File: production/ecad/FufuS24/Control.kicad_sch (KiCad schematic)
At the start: 28 parts, among them IC1 NLVPCA9535EDTR2G, J2 Conn_01x02, U1 RP2040, U2 W25Q128JVS

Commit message: Made GPIO changes
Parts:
- removed R29: 4.7k, footprints:RESC2012X60N, symbol Device:R
- added R24: 4.7k, footprints:RESC2012X60N, symbol Device:R
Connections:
- net +3.3V: now also R24.1
- net Heat_PWM1: now also U1.31 (GPIO20); no longer IC1.18 (IO1_5)
- net SCL_EXT: now also R19.2
- net SDA_EXT: now also R24.2
- net Watersense1_Mode: now also IC1.10 (IO0_6); no longer U1.32 (GPIO21)
- net Watersense1_Read: now also IC1.11 (IO0_7); no longer U1.31 (GPIO20)
- net Watersense2_Mode: now also IC1.8 (IO0_4); no longer U1.35 (GPIO23)
- net Watersense2_Read: now also IC1.9 (IO0_5); no longer U1.34 (GPIO22)
- net I2C0_SCL: no longer names the net of IC1.19 (IO1_6)
- net I2C0_SDA: no longer names the net of IC1.20 (IO1_7)
- net I2C0_SDA: no longer R19.2
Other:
- moved on the sheet: IC1

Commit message: Big layout push
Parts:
- removed IC1: NLVPCA9535EDTR2G, footprints:SOP65P640X120-24N, symbol NLVPCA9535EDTR2G:NLVPCA9535EDTR2G
- removed R41, R42: 1.75k, footprints:RESC2012X60N, symbol Device:R
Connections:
- net AD0_EXT is gone; now on net Piezo_Enable: U1.4 (GPIO2)
- net AD2_EXT is gone; now on net Motor_BIN1: U1.6 (GPIO4)
- net I2C1_SCL_DVI is gone; now on net HOT_LED_NEG: U1.30 (GPIO19)
- net I2C1_SDA_DVI is gone; now on net HOT_LED_POS: U1.29 (GPIO18)
- net Pump_Enable: now also U1.32 (GPIO21)
- net Watersense1_Read: now also U1.35 (GPIO23)
- net Watersense2_Read: now also U1.34 (GPIO22)
- net AD1_EXT: no longer names the net of U1.5 (GPIO3)

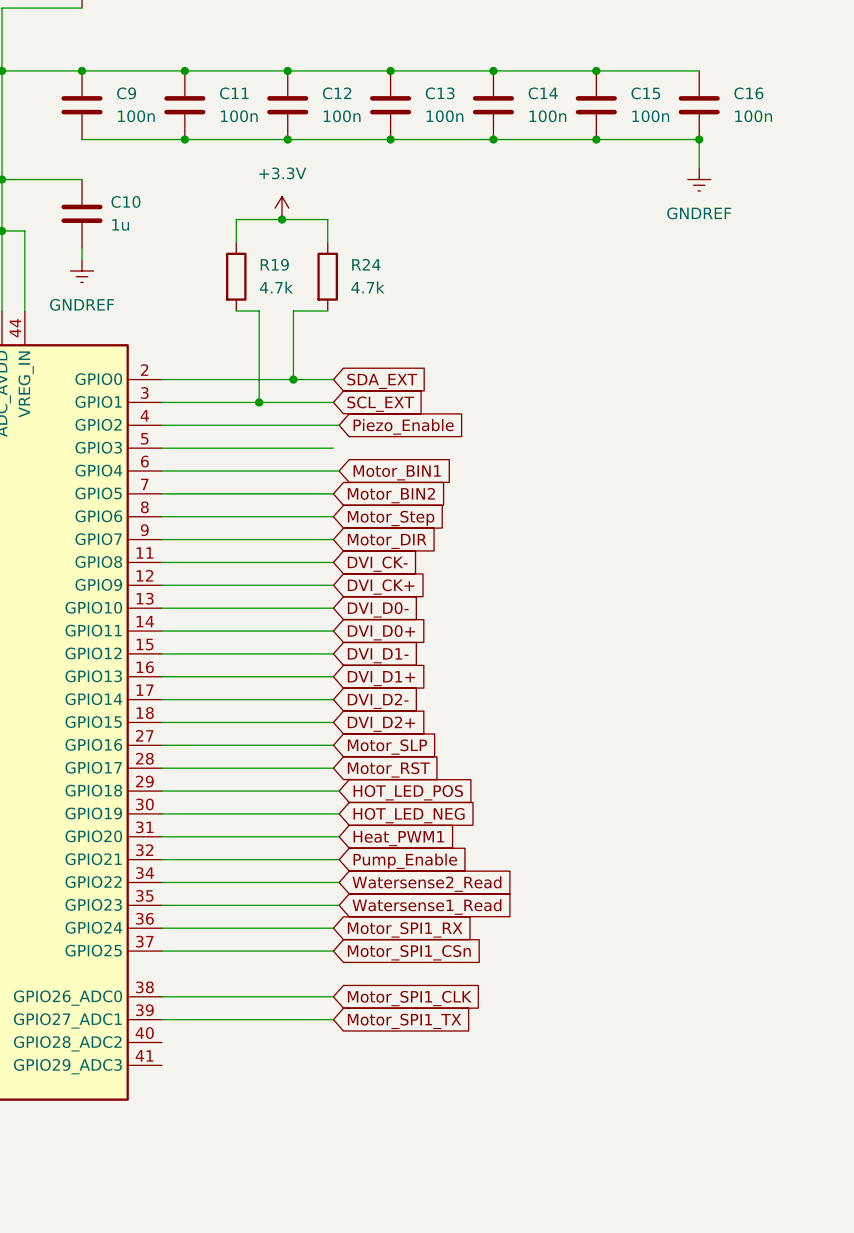
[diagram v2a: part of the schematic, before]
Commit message: major layout changes
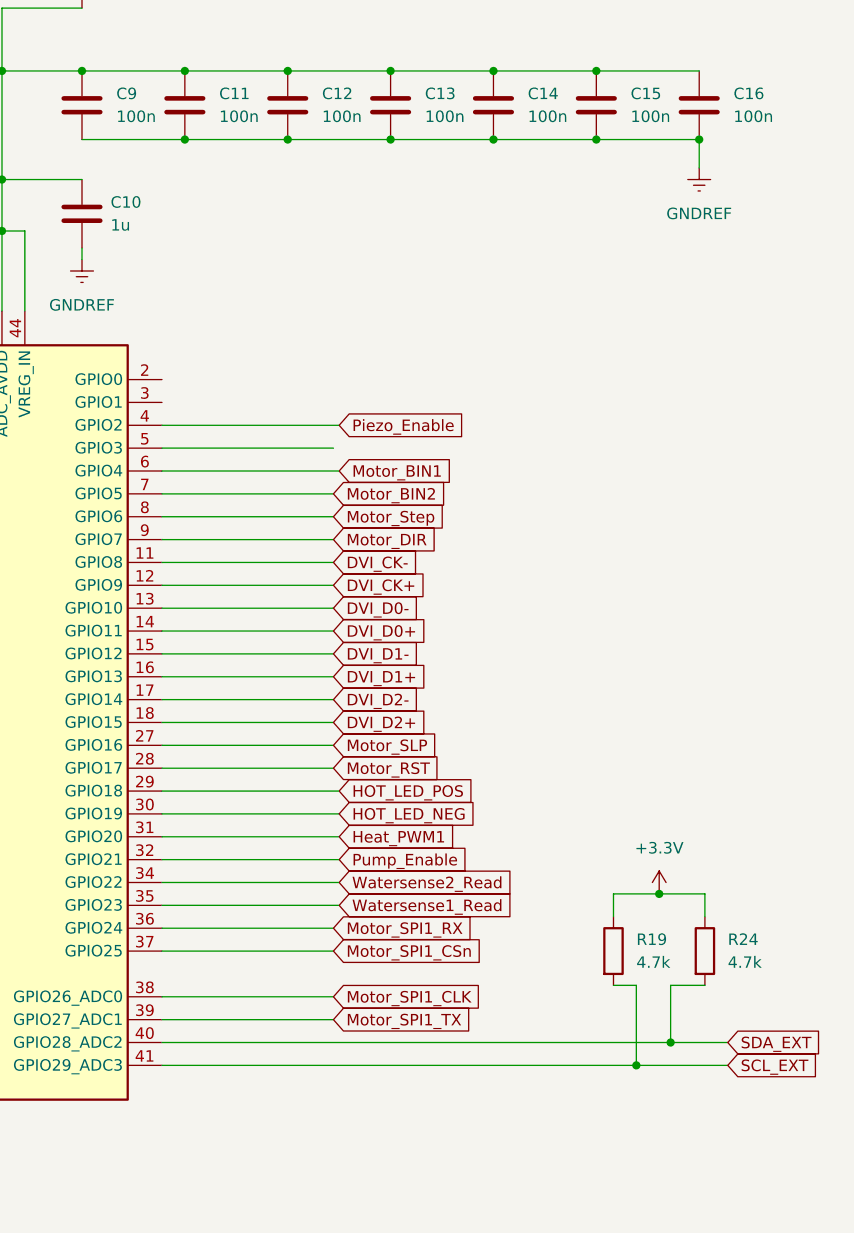
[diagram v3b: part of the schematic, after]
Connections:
- net SCL_EXT: now also U1.41 (GPIO29_ADC3); no longer U1.3 (GPIO1)
- net SDA_EXT: now also U1.40 (GPIO28_ADC2); no longer U1.2 (GPIO0)

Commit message: HDMI + USB
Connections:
- net DVI_CK+: now also U1.11 (GPIO8); no longer U1.12 (GPIO9)
- net DVI_CK-: now also U1.12 (GPIO9); no longer U1.11 (GPIO8)
- net DVI_D1+: now also U1.15 (GPIO12); no longer U1.16 (GPIO13)
- net DVI_D1-: now also U1.16 (GPIO13); no longer U1.15 (GPIO12)
- net DVI_D2+: now also U1.17 (GPIO14); no longer U1.18 (GPIO15)
- net DVI_D2-: now also U1.18 (GPIO15); no longer U1.17 (GPIO14)
- net USB_DP: now reaches R3.2, U1.47 (USB_DP)
- net USB_DN: now reaches R4.2, U1.46 (USB_DM)
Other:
- moved on the sheet: R3, R4
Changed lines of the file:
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@@
-    (stroke (width 0) (type default))
-  )
-  (wire (pts (xy 86.995 77.47) (xy 92.075 77.47))
     (stroke (width 0) (type default))
   )
@@
     (stroke (width 0) (type default))
   )
-  (wire (pts (xy 86.995 80.01) (xy 92.075 80.01))
-    (stroke (width 0) (type default))
-  )
   (wire (pts (xy 33.02 81.915) (xy 38.1 81.915))
     (stroke (width 0) (type default))
@@
   )
   (wire (pts (xy 125.095 47.625) (xy 125.095 53.34))
-    (stroke (width 0) (type default))
-  )
-  (wire (pts (xy 86.995 70.485) (xy 86.995 77.47))
     (stroke (width 0) (type default))
   )
@@
     )
   )
-  (global_label "USB_D-" (shape input) (at 79.375 80.01 180) (fields_autoplaced)
+  (global_label "USB_D-" (shape input) (at 71.12 85.09 180) (fields_autoplaced)
     (effects (font (size 1.27 1.27)) (justify right))
-    (property "Intersheetrefs" "${INTERSHEET_REFS}" (at 68.7698 80.01 0)
+    (property "Intersheetrefs" "${INTERSHEET_REFS}" (at 60.5148 85.09 0)
       (effects (font (size 1.27 1.27)) (justify right) hide)
     )
@@
     )
   )
-  (global_label "USB_D+" (shape input) (at 79.375 70.485 180) (fields_autoplaced)
+  (global_label "USB_D+" (shape input) (at 69.85 73.025 180) (fields_autoplaced)
     (effects (font (size 1.27 1.27)) (justify right))
-    (property "Intersheetrefs" "${INTERSHEET_REFS}" (at 68.7698 70.485 0)
+    (property "Intersheetrefs" "${INTERSHEET_REFS}" (at 59.2448 73.025 0)
       (effects (font (size 1.27 1.27)) (justify right) hide)
     )
   )
+  (global_label "USB_DN" (shape input) (at 92.075 80.01 180) (fields_autoplaced)
+    (effects (font (size 1.27 1.27)) (justify right))
+    (property "Intersheetrefs" "${INTERSHEET_REFS}" (at 81.7117 80.01 0)
+      (effects (font (size 1.27 1.27)) (justify right) hide)
+    )
+  )
   (global_label "Motor_SPI1_RX" (shape input) (at 161.925 130.81 0) (fields_autoplaced)
     (effects (font (size 1.27 1.27)) (justify left))
@@
     )
   )
+  (global_label "USB_DP" (shape input) (at 77.47 73.025 0) (fields_autoplaced)
+    (effects (font (size 1.27 1.27)) (justify left))
+    (property "Intersheetrefs" "${INTERSHEET_REFS}" (at 87.7728 73.025 0)
+      (effects (font (size 1.27 1.27)) (justify left) hide)
+    )
+  )
   (global_label "Motor_BIN1" (shape input) (at 162.56 80.01 0) (fields_autoplaced)
     (effects (font (size 1.27 1.27)) (justify left))
@@
     )
   )
+  (global_label "USB_DN" (shape input) (at 78.74 85.09 0) (fields_autoplaced)
+    (effects (font (size 1.27 1.27)) (justify left))
+    (property "Intersheetrefs" "${INTERSHEET_REFS}" (at 89.1033 85.09 0)
+      (effects (font (size 1.27 1.27)) (justify left) hide)
+    )
+  )
   (global_label "Motor_BIN2" (shape input) (at 161.925 82.55 0) (fields_autoplaced)
     (effects (font (size 1.27 1.27)) (justify left))
@@
     )
   )
-  (global_label "DVI_CK+" (shape input) (at 161.925 92.71 0) (fields_autoplaced)
+  (global_label "DVI_CK-" (shape input) (at 161.925 92.71 0) (fields_autoplaced)
     (effects (font (size 1.27 1.27)) (justify left))
     (property "Intersheetrefs" "${INTERSHEET_REFS}" (at 172.9536 92.71 0)
@@
     )
   )
-  (global_label "DVI_D1+" (shape input) (at 161.925 102.87 0) (fields_autoplaced)
+  (global_label "DVI_D1-" (shape input) (at 161.925 102.87 0) (fields_autoplaced)
     (effects (font (size 1.27 1.27)) (justify left))
     (property "Intersheetrefs" "${INTERSHEET_REFS}" (at 172.8931 102.87 0)
@@
     )
   )
-  (global_label "DVI_CK-" (shape input) (at 161.925 90.17 0) (fields_autoplaced)
+  (global_label "DVI_CK+" (shape input) (at 161.925 90.17 0) (fields_autoplaced)
     (effects (font (size 1.27 1.27)) (justify left))
     (property "Intersheetrefs" "${INTERSHEET_REFS}" (at 172.9536 90.17 0)
@@
     )
   )
-  (global_label "DVI_D2-" (shape input) (at 161.925 105.41 0) (fields_autoplaced)
+  (global_label "DVI_D2+" (shape input) (at 161.925 105.41 0) (fields_autoplaced)
     (effects (font (size 1.27 1.27)) (justify left))
     (property "Intersheetrefs" "${INTERSHEET_REFS}" (at 172.8931 105.41 0)
@@
     )
   )
-  (global_label "DVI_D1-" (shape input) (at 161.925 100.33 0) (fields_autoplaced)
+  (global_label "DVI_D1+" (shape input) (at 161.925 100.33 0) (fields_autoplaced)
     (effects (font (size 1.27 1.27)) (justify left))
     (property "Intersheetrefs" "${INTERSHEET_REFS}" (at 172.8931 100.33 0)
@@
     )
   )
-  (global_label "DVI_D2+" (shape input) (at 161.925 107.95 0) (fields_autoplaced)
+  (global_label "DVI_D2-" (shape input) (at 161.925 107.95 0) (fields_autoplaced)
     (effects (font (size 1.27 1.27)) (justify left))
     (property "Intersheetrefs" "${INTERSHEET_REFS}" (at 172.8931 107.95 0)
@@
     (property "Intersheetrefs" "${INTERSHEET_REFS}" (at 182.9622 125.73 0)
       (effects (font (size 1.27 1.27)) (justify left) hide)
+    )
+  )
+  (global_label "USB_DP" (shape input) (at 92.075 77.47 180) (fields_autoplaced)
+    (effects (font (size 1.27 1.27)) (justify right))
+    (property "Intersheetrefs" "${INTERSHEET_REFS}" (at 81.7722 77.47 0)
+      (effects (font (size 1.27 1.27)) (justify right) hide)
     )
   )
@@
     )
   )
-  (symbol (lib_id "Device:R_US") (at 83.185 70.485 90) (unit 1)
-    (in_bom yes) (on_board yes) (dnp no) (fields_autoplaced)
-    (property "Reference" "R3" (at 83.185 64.135 90)
-      (effects (font (size 1.27 1.27)))
-    )
-    (property "Value" "27.4" (at 83.185 66.675 90)
-      (effects (font (size 1.27 1.27)))
-    )
-    (property "Footprint" "footprints:RESC2012X60N" (at 83.439 69.469 90)
-      (effects (font (size 1.27 1.27)) hide)
-    )
-    (property "Datasheet" "~" (at 83.185 70.485 0)
+  (symbol (lib_id "Device:R_US") (at 73.66 73.025 90) (unit 1)
+    (in_bom yes) (on_board yes) (dnp no) (fields_autoplaced)
+    (property "Reference" "R3" (at 73.66 66.675 90)
+      (effects (font (size 1.27 1.27)))
+    )
+    (property "Value" "27.4" (at 73.66 69.215 90)
+      (effects (font (size 1.27 1.27)))
+    )
+    (property "Footprint" "footprints:RESC2012X60N" (at 73.914 72.009 90)
+      (effects (font (size 1.27 1.27)) hide)
+    )
+    (property "Datasheet" "~" (at 73.66 73.025 0)
       (effects (font (size 1.27 1.27)) hide)
     )
@@
     )
   )
-  (symbol (lib_id "Device:R_US") (at 83.185 80.01 90) (unit 1)
-    (in_bom yes) (on_board yes) (dnp no) (fields_autoplaced)
-    (property "Reference" "R4" (at 83.185 74.295 90)
-      (effects (font (size 1.27 1.27)))
-    )
-    (property "Value" "27.4" (at 83.185 76.835 90)
-      (effects (font (size 1.27 1.27)))
-    )
-    (property "Footprint" "footprints:RESC2012X60N" (at 83.439 78.994 90)
-      (effects (font (size 1.27 1.27)) hide)
-    )
-    (property "Datasheet" "~" (at 83.185 80.01 0)
-      (effects (font (size 1.27 1.27)) hide)
-    )
+  (symbol (lib_id "Device:R_US") (at 74.93 85.09 90) (unit 1)
+    (in_bom yes) (on_board yes) (dnp no) (fields_autoplaced)
+    (property "Reference" "R4" (at 74.93 79.375 90)
+      (effects (font (size 1.27 1.27)))
+    )
+    (property "Value" "27.4" (at 74.93 81.915 90)
+      (effects (font (size 1.27 1.27)))
+    )
+    (property "Footprint" "footprints:RESC2012X60N" (at 75.184 84.074 90)
+      (effects (font (size 1.27 1.27)) hide)
+    )
+    (property "Datasheet" "~" (at 74.93 85.09 0)
+      (effects (font (size 1.27 1.27)) hide)
+    )

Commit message: review changes
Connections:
- net HOT_LED_NEG: no longer names the net of U1.30 (GPIO19)
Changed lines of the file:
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@@
-    (stroke (width 0) (type default))
-  )
-  (wire (pts (xy 142.875 118.11) (xy 162.56 118.11))
     (stroke (width 0) (type default))
   )
@@
       (effects (font (size 1.27 1.27)) (justify left) hide)
     )
-  )
-  (global_label "HOT_LED_NEG" (shape input) (at 162.56 118.11 0) (fields_autoplaced)
-    (effects (font (size 1.27 1.27)) (justify left))
-    (property "Intersheetrefs" "${INTERSHEET_REFS}" (at 178.3056 118.11 0)
-      (effects (font (size 1.27 1.27)) (justify left) hide)
-    )

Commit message: i am pulling my hair out
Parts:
- added J14, J15, J16: 691137710004, footprints:PWR_4POS, symbol PWR_4POS:691137710004
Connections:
- net GPIO_19: now reaches U1.30 (GPIO19)
- net GPIO_19: now also J15.1
- net GPIO_3: now reaches U1.5 (GPIO3)
- net Motor_BIN1 renamed Motor_PWM
- net Motor_BIN2 renamed GPIO_4
- net Motor_DIR renamed GPIO_6
- net GPIO_6: now also J14.1
- net Motor_RST renamed GPIO_8
- net GPIO_8: now also J14.3
- net Motor_SLP renamed GPIO_7
- net GPIO_7: now also J14.4
- net Motor_SPI1_CLK renamed GPIO_26
- net GPIO_26: now also J15.4
- net Motor_SPI1_CSn renamed GPIO_25
- net GPIO_25: now also J15.2
- net Motor_SPI1_RX renamed GPIO_24
- net GPIO_24: now also J15.3
- net Motor_SPI1_TX renamed GPIO_27
- net GPIO_27: now also J16.1
- net Motor_Step renamed GPIO_5
- net GPIO_5: now also J14.2

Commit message: changes
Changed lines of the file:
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@@
+    (stroke (width 0) (type default))
+  )
+  (wire (pts (xy 162.56 118.11) (xy 142.875 118.11))
     (stroke (width 0) (type default))
   )
@@
     )
   )
-  (global_label "GPIO_19" (shape input) (at 142.875 118.11 0) (fields_autoplaced)
-    (effects (font (size 1.27 1.27)) (justify left))
-    (property "Intersheetrefs" "${INTERSHEET_REFS}" (at 153.7221 118.11 0)
-      (effects (font (size 1.27 1.27)) (justify left) hide)
-    )
+  (global_label "GPIO_19" (shape input) (at 162.56 118.11 0) (fields_autoplaced)
+    (effects (font (size 1.27 1.27)) (justify left))
+    (property "Intersheetrefs" "${INTERSHEET_REFS}" (at 173.4071 118.11 0)
+      (effects (font (size 1.27 1.27)) (justify left) hide)
+    )

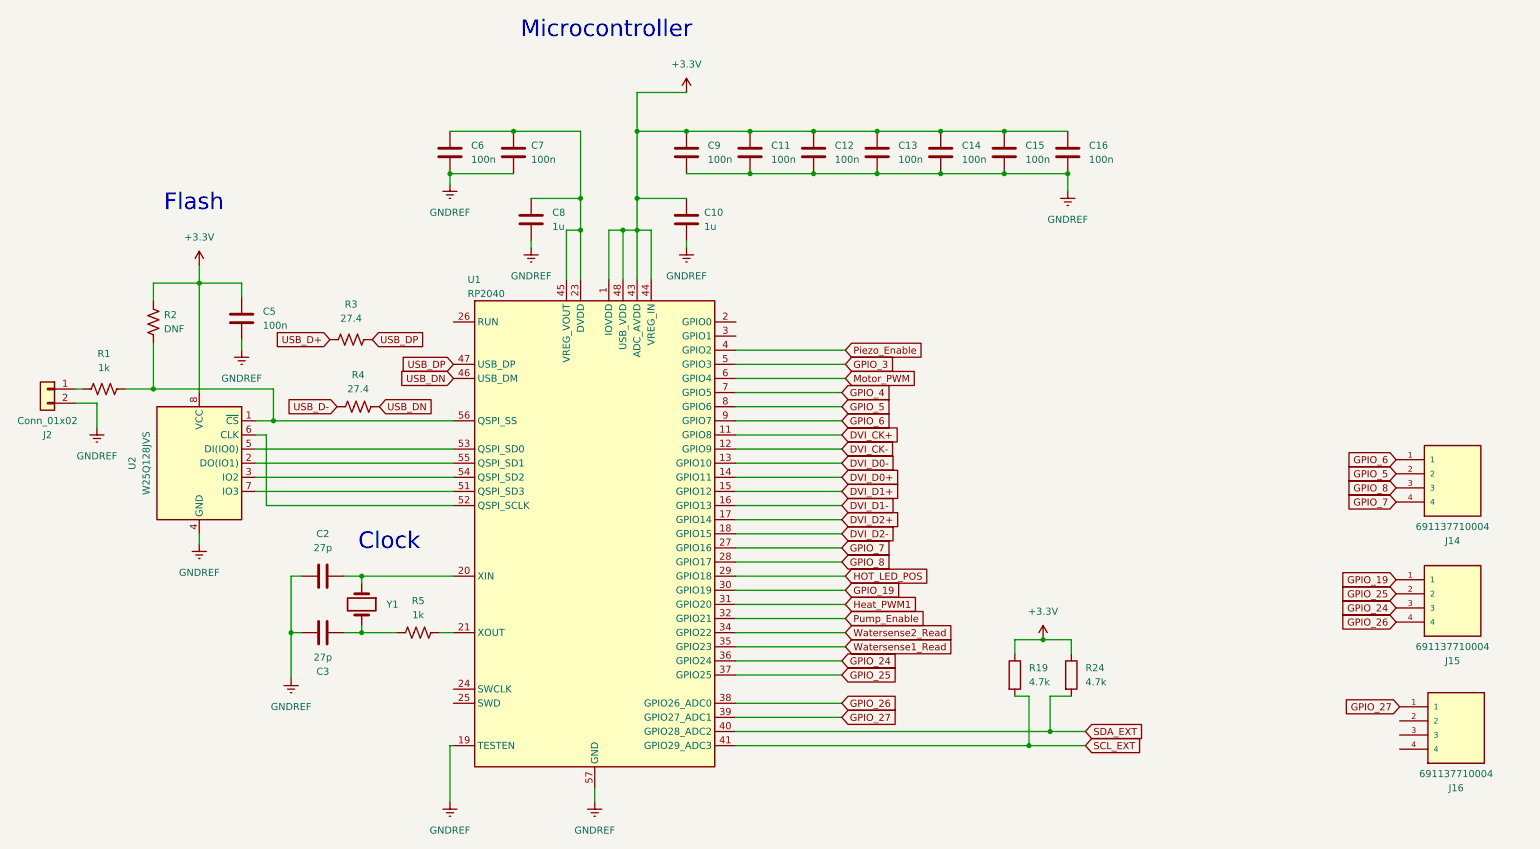
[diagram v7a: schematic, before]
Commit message: updated layout
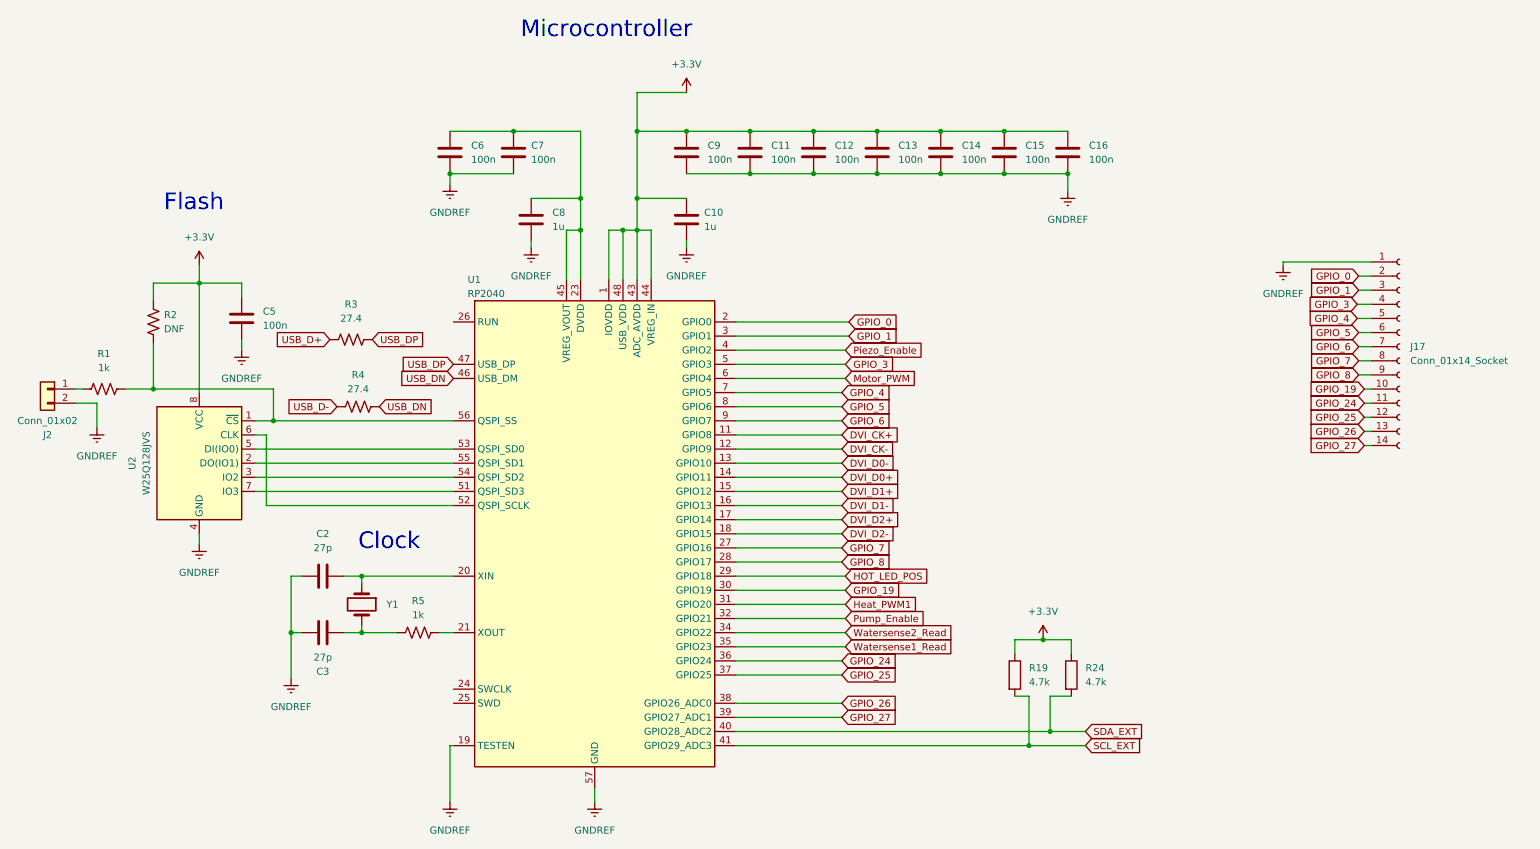
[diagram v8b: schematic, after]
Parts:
- removed J14, J15, J16: 691137710004, footprints:PWR_4POS, symbol PWR_4POS:691137710004
- added J17: Conn_01x14_Socket, Connector_PinSocket_2.54mm:PinSocket_1x14_P2.54mm_Vertical, symbol Connector:Conn_01x14_Socket
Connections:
- net GNDREF: now also J17.1 (Pin_1)
- net GPIO_19: now also J17.10 (Pin_10)
- net GPIO_24: now also J17.11 (Pin_11)
- net GPIO_25: now also J17.12 (Pin_12)
- net GPIO_26: now also J17.13 (Pin_13)
- net GPIO_27: now also J17.14 (Pin_14)
- net GPIO_3: now also J17.4 (Pin_4)
- net GPIO_4: now also J17.5 (Pin_5)
- net GPIO_5: now also J17.6 (Pin_6)
- net GPIO_6: now also J17.7 (Pin_7)
- net GPIO_7: now also J17.8 (Pin_8)
- net GPIO_8: now also J17.9 (Pin_9)
- net GPIO_0: now reaches U1.2 (GPIO0)
- net GPIO_0: now also J17.2 (Pin_2)
- net GPIO_1: now reaches U1.3 (GPIO1)
- net GPIO_1: now also J17.3 (Pin_3)
